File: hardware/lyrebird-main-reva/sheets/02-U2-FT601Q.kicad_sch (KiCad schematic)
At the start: 17 parts, among them U2 FT601Q, Y1 ABM8G-30.000MHZ-18-D2Y-T

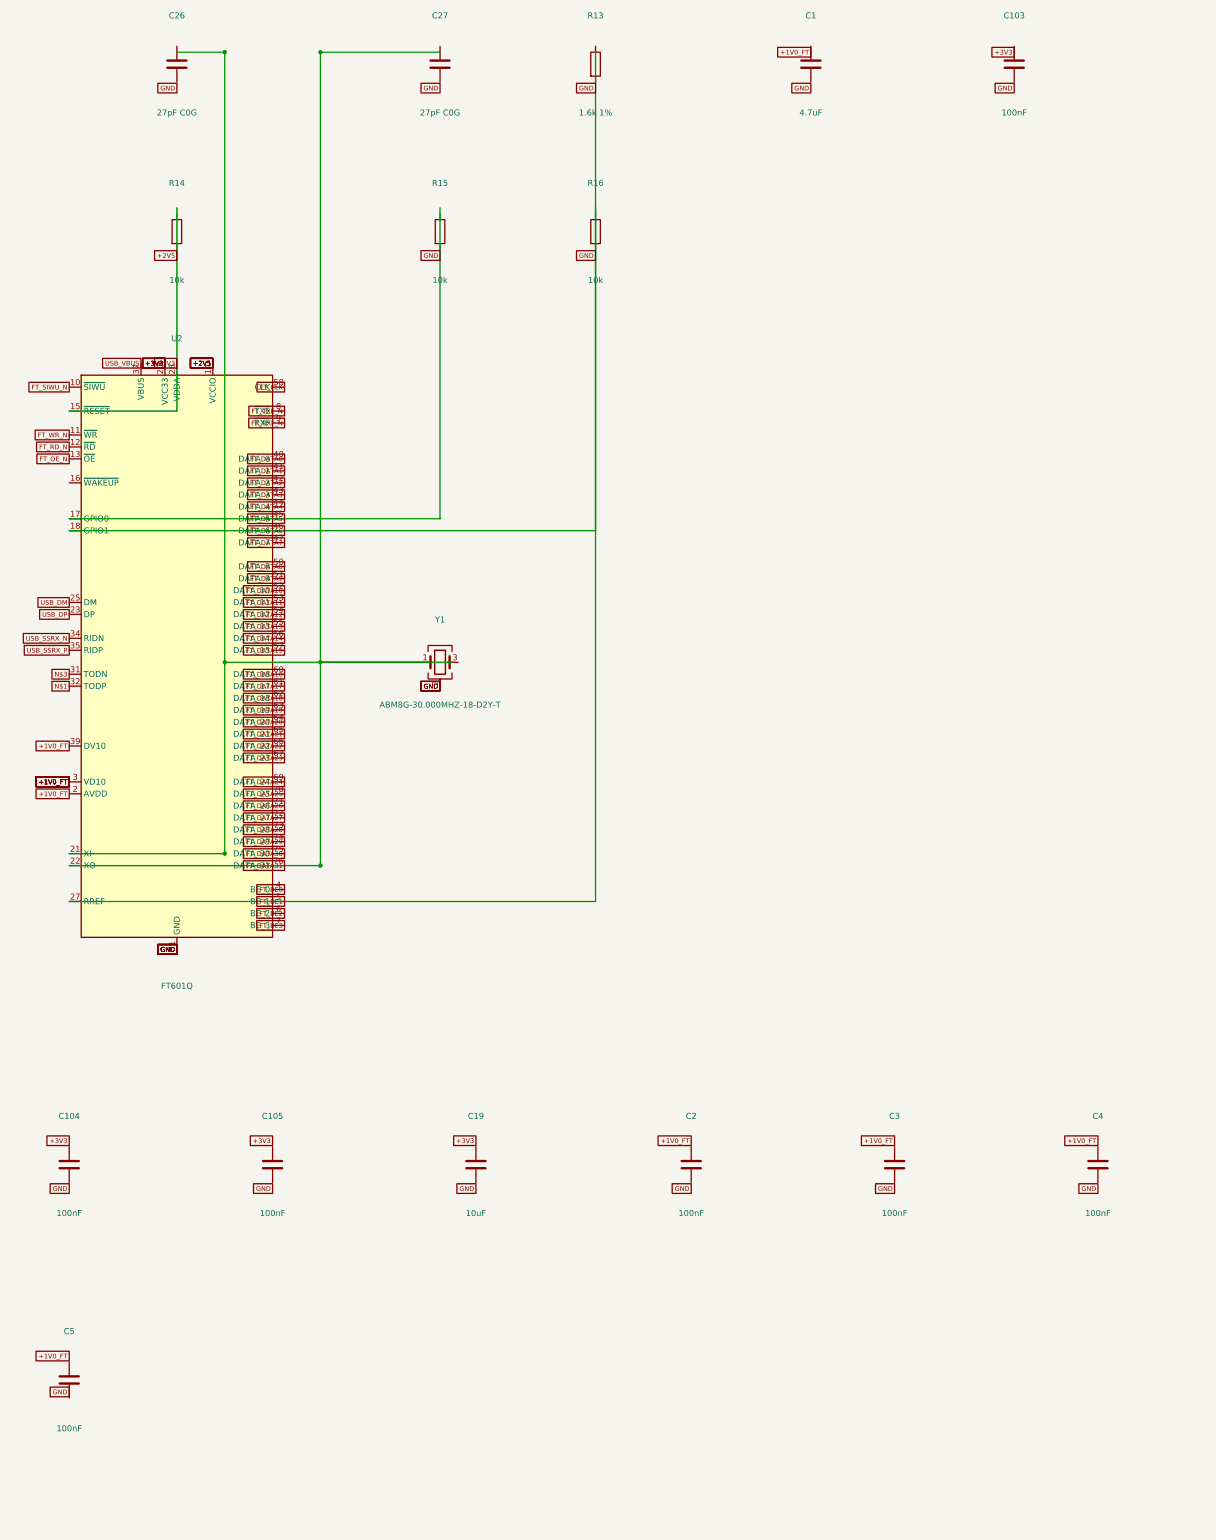
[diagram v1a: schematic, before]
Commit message: Act on the schematic validation: three faults and the core-rail guard
**The SuperSpeed pairs were wired backwards, and are now not wired.**
USB_SSRX_P/N were the only multi-node nets on the board with an INPUT at
every pin -- the receptacle's SSRX pins are inputs and so are the
bridge's RIDP/RIDN, so nothing drove them, and the transmit pair was
mirrored the same way. The comment asserted a crossover inside the cable
as fact and reasoned from it; USB 3.0 cables have no crossover.
SuperSpeed would never have trained and the link would have fallen back
to 480 Mb/s silently -- which is the speed 0014 chose on purpose, since
no galvanic isolator exists above USB 2.0. So the pairs are removed
rather than corrected, which also retires the hardest constraint in this
board's layout. How to wire them correctly if they ever come back is
recorded where they were.

**The inverting converter had no input capacitor across its own
terminals.** Nothing spanned +12V and -6V_A, and U7's GND pin *is*
-6V_A, so the loop its switching current actually takes was unbypassed
-- the input caps near U5 are referenced to system ground and are not in
that loop at all. This is the third fault found in U7 and all three are
the same mistake: reasoning about it as though its ground were the
board's.

**The translator's output enables are tied low against an explicit
datasheet instruction**, and the fix is sequencing rather than a pull-up.
SCES576I says OE must be pulled up to VCCA and not enabled until both
supplies are stable; a pull-up is not available here because nothing on
the module could pull it down -- no spare mezzanine pin, and MUTE_N has
the wrong polarity. Instead VCC(A) is made the last rail to arrive:
10 uF on U9's SET gives 573 ms against 359 ms for VCC(B), so the enable
cannot precede the supply it switches to. It costs nothing, because that
rail feeds the translator's reference supply and nothing else.

**The core rail now has a guard, and it needed two attempts.** The
existing as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
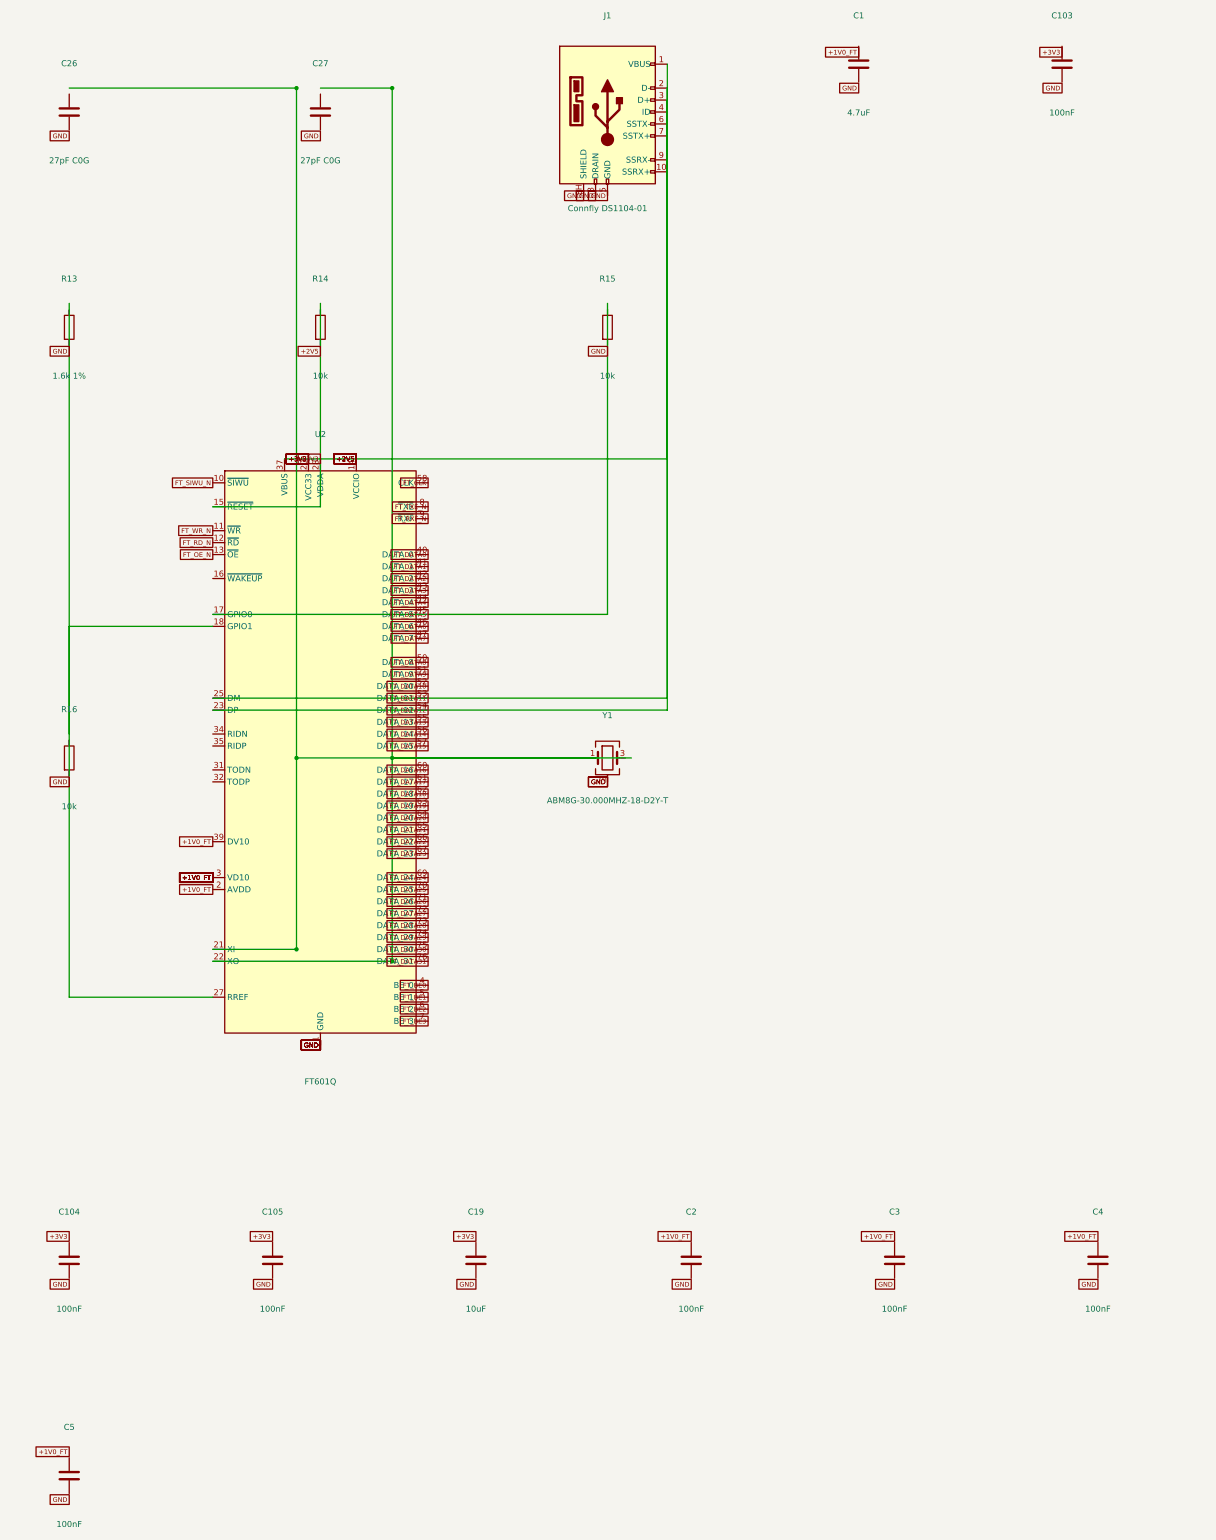
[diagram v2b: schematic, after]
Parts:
- added C5: 100nF, symbol Device:C
- C1: renamed from C103; value 100nF -> 4.7uF
- C105: renamed from C19; value 10uF -> 100nF
- C19: renamed from C2; value 100nF -> 10uF
- J1: renamed from R13; value 1.6k 1% -> Connfly DS1104-01; symbol Device:R -> Connector:USB3_B_Micro
- R13: renamed from R14; value 10k -> 1.6k 1%
- R16: renamed from U2; value FT601Q -> 10k; symbol Interface_USB:FT601Q -> Device:R
- U2: renamed from Y1; value ABM8G-30.000MHZ-18-D2Y-T -> FT601Q; symbol Device:Crystal_GND24 -> Interface_USB:FT601Q
- Y1: renamed from C1; value 4.7uF -> ABM8G-30.000MHZ-18-D2Y-T; symbol Device:C -> Device:Crystal_GND24
- renumbered C104 to C103, C105 to C104, C3 to C2, C4 to C3, C5 to C4, R15 to R14, R16 to R15
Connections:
- net +1V0_FT: now also U2.2 (AVDD), U2.3 (VD10), U2.30 (VD10), U2.33 (VD10), U2.39 (DV10), U2.48 (VD10); no longer R16.2 (AVDD), R16.3 (VD10), R16.30 (VD10), R16.33 (VD10), R16.39 (DV10), R16.48 (VD10)
- net +2V5: now also J1.1 (VBUS), J1.2 (D-), J1.3 (D+), U2.14 (VCCIO), U2.15 (~{RESET}), U2.20 (VCC33), U2.23 (DP), U2.24 (VCC33), U2.25 (DM), U2.28 (VDDA), U2.37 (VBUS), U2.38 (VCC33), U2.49 (VCCIO), U2.53 (DATA_11), U2.54 (DATA_12), U2.59 (VCCIO), U2.68 (VCCIO); no longer R16.14 (VCCIO), R16.15 (~{RESET}), R16.20 (VCC33), R16.24 (VCC33), R16.28 (VDDA), R16.38 (VCC33), R16.49 (VCCIO), R16.59 (VCCIO), R16.68 (VCCIO)
- net FT_BE0: now also U2.4 (BE_0); no longer R16.4 (BE_0)
- net FT_BE1: now also U2.5 (BE_1); no longer R16.1 (GND), R16.17 (GPIO0), R16.18 (GPIO1), R16.26 (GND), R16.27 (RREF), R16.29 (GND), R16.36 (GND), R16.45 (DATA_5), R16.46 (DATA_6), R16.5 (BE_1), R16.77 (GND), U2.2 (G), U2.4 (G)
- net FT_BE2: now also U2.6 (BE_2); no longer R16.6 (BE_2)
- net FT_BE3: now also U2.7 (BE_3); no longer R16.7 (BE_3)
- net FT_CLK: now also U2.58 (CLK); no longer R16.58 (CLK)
- net FT_DATA0: now also U2.40 (DATA_0); no longer R16.40 (DATA_0)
- net FT_DATA1: now also U2.41 (DATA_1); no longer R16.41 (DATA_1)
- net FT_DATA10: now also U2.52 (DATA_10); no longer R16.52 (DATA_10)
- net FT_DATA13: now also U2.55 (DATA_13); no longer R16.55 (DATA_13)
- net FT_DATA14: now also U2.56 (DATA_14); no longer R16.56 (DATA_14)
- net FT_DATA15: now also U2.57 (DATA_15); no longer R16.57 (DATA_15)
- net FT_DATA16: now also U2.60 (DATA_16); no longer R16.60 (DATA_16)
- net FT_DATA17: now also U2.61 (DATA_17); no longer R16.61 (DATA_17)
- net FT_DATA18: now also U2.62 (DATA_18); no longer R16.62 (DATA_18)
- net FT_DATA19: now also U2.63 (DATA_19); no longer R16.63 (DATA_19)
- net FT_DATA2: now also U2.42 (DATA_2); no longer R16.42 (DATA_2)
- net FT_DATA20: now also U2.64 (DATA_20); no longer R16.64 (DATA_20)
- net FT_DATA21: now also U2.65 (DATA_21); no longer R16.65 (DATA_21)
- net FT_DATA22: now also U2.66 (DATA_22); no longer R16.66 (DATA_22)
- net FT_DATA23: now also U2.67 (DATA_23); no longer R16.67 (DATA_23)
- net FT_DATA24: now also U2.69 (DATA_24); no longer R16.69 (DATA_24)
- net FT_DATA25: now also U2.70 (DATA_25); no longer R16.70 (DATA_25)
- net FT_DATA26: now also U2.71 (DATA_26); no longer R16.71 (DATA_26)
- net FT_DATA27: now also U2.72 (DATA_27); no longer R16.72 (DATA_27)
- net FT_DATA28: now also U2.73 (DATA_28); no longer R16.73 (DATA_28)
- net FT_DATA29: now also U2.74 (DATA_29); no longer R16.74 (DATA_29)
- net FT_DATA3: now also U2.43 (DATA_3); no longer R16.43 (DATA_3)
- net FT_DATA30: now also U2.75 (DATA_30); no longer R16.75 (DATA_30)
- net FT_DATA31: now also U2.76 (DATA_31); no longer R16.21 (XI), R16.22 (XO), R16.76 (DATA_31)
- net FT_DATA4: now also U2.44 (DATA_4); no longer R16.44 (DATA_4)
- net FT_DATA7: now also U2.47 (DATA_7); no longer R16.47 (DATA_7)
- net FT_DATA8: now also U2.50 (DATA_8); no longer R16.50 (DATA_8)
- net FT_DATA9: now also U2.51 (DATA_9); no longer R16.51 (DATA_9)
- net FT_OE_N: now also U2.13 (~{OE}); no longer R16.13 (~{OE})
- net FT_RD_N: now also U2.12 (~{RD}); no longer R16.12 (~{RD})
- net FT_RXF_N: now also U2.9 (~{RXF}); no longer R16.9 (~{RXF})
- net FT_SIWU_N: now also U2.10 (~{SIWU}); no longer R16.10 (~{SIWU})
- net FT_TXE_N: now also U2.8 (~{TXE}); no longer R16.8 (~{TXE})
- net FT_WR_N: now also U2.11 (~{WR}); no longer R16.11 (~{WR})
- net FT_DATA5: now reaches U2.1 (GND)
- net FT_DATA5: now also J1.5 (GND), J1.8 (DRAIN), J1.SH (SHIELD), U2.17 (GPIO0), U2.18 (GPIO1), U2.26 (GND), U2.27 (RREF), U2.29 (GND), U2.36 (GND), U2.45 (DATA_5), U2.77 (GND), Y1.2 (G), Y1.4 (G)
- removed net FT_DATA11: R16.53 (DATA_11)
- removed net FT_DATA12: R16.54 (DATA_12)
- removed net N$1: R16.32 (TODP)
- removed net N$3: R16.31 (TODN)
- removed net USB_DM: R16.25 (DM)
- removed net USB_DP: R16.23 (DP)
- removed net USB_SSRX_N: R16.34 (RIDN)
- removed net USB_SSRX_P: R16.35 (RIDP)
- removed net USB_VBUS: R16.37 (VBUS)
- new net: U2.21 (XI), U2.22 (XO)
- new net FT_DATA6: U2.46 (DATA_6)
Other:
- moved on the sheet: C1, C103, C104, C105, C19, C2, C26, C27, C3, C4, R13, R14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
